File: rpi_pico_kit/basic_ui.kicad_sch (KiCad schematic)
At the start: 47 parts, among them Q3 BSS138, Q4 BSS138, Q5 BSS138, Q6 BSS138, SW2 RotaryEncoder_Switch, SW3 SW_Push_Dual, SW4 SW_Push_Dual, SW5 SW_Push_Dual, SW6 SW_Push_Dual, U5 74HC14

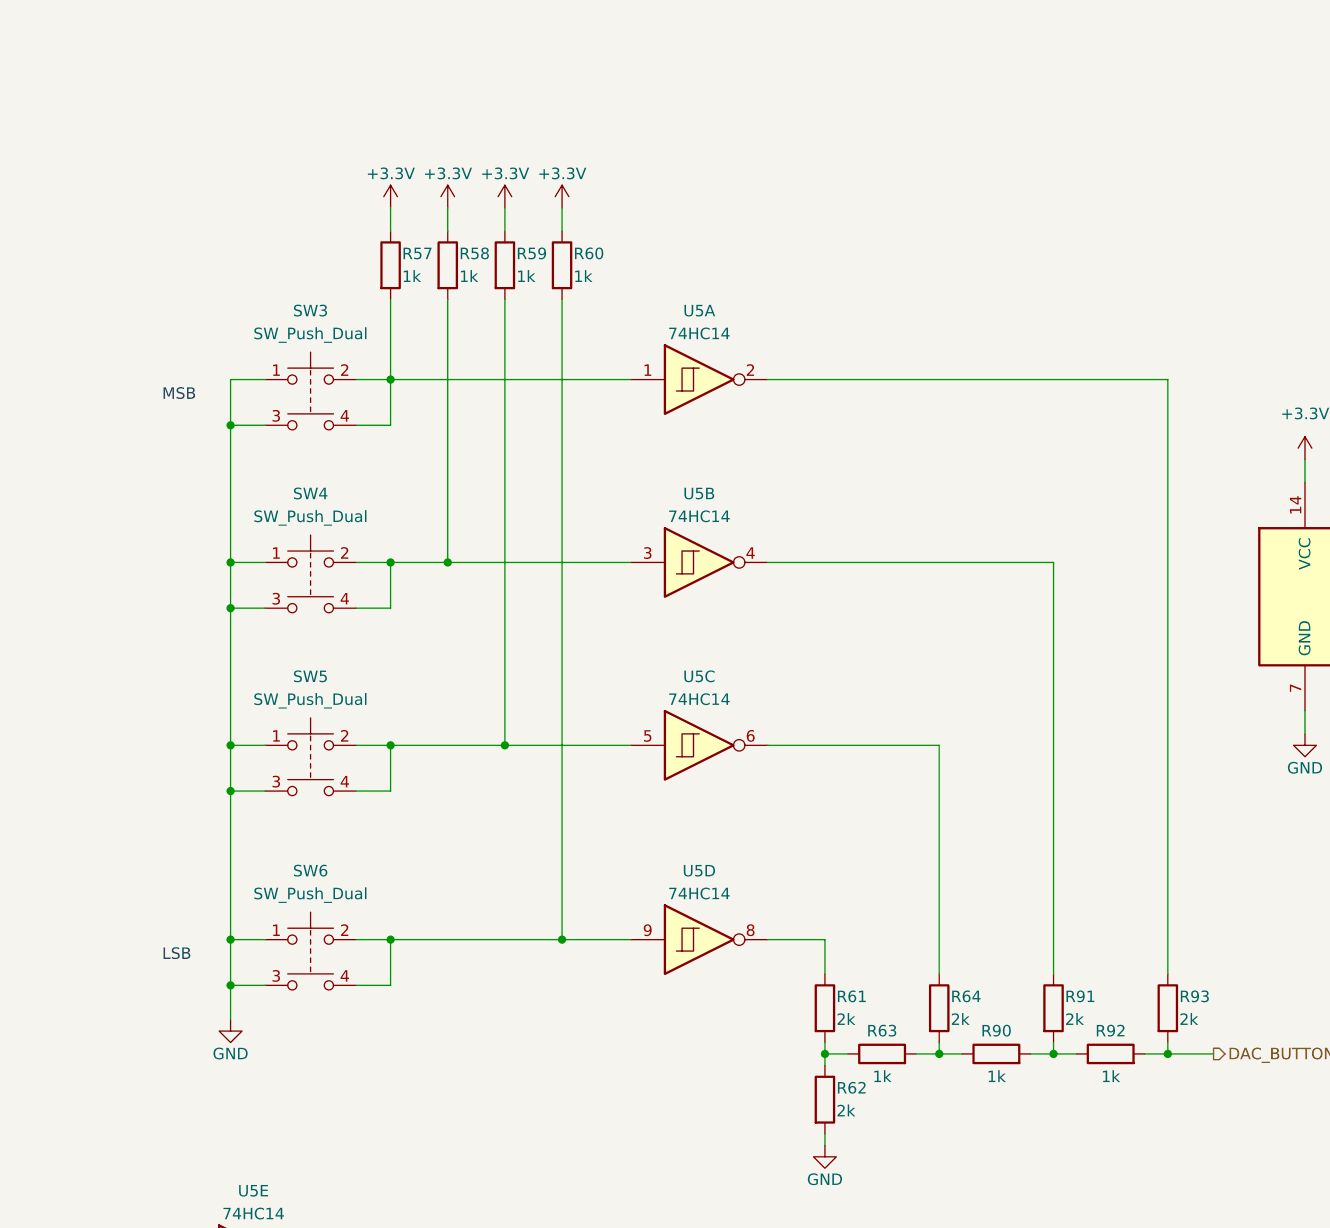
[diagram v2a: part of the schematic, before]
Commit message: replaced buttons in schematic
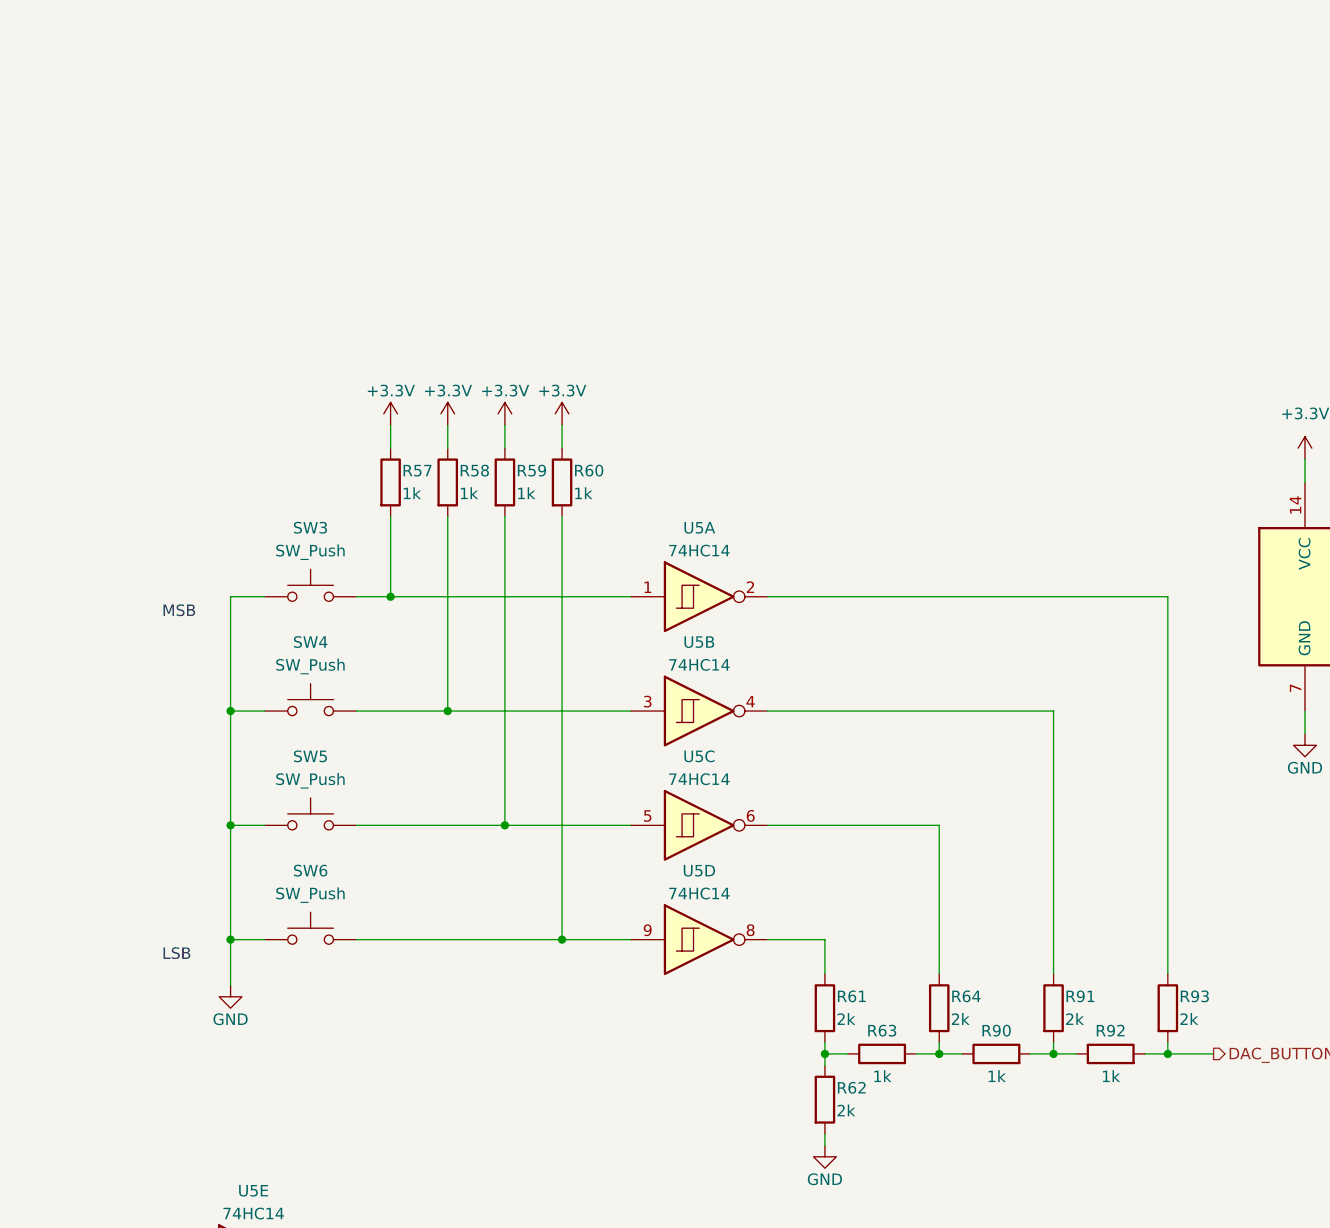
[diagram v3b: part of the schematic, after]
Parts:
- removed SW3, SW4, SW5, SW6: SW_Push_Dual, symbol Switch:SW_Push_Dual
- added SW3, SW4, SW5, SW6: SW_Push, Button_Switch_THT:SW_TH_Tactile_Omron_B3F-10xx, symbol Switch:SW_Push
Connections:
- net GND: now also SW3.1, SW4.1, SW5.1, SW6.1
- net at R60.2, U5.9: now also SW6.2
- net at R58.2, U5.3: now also SW4.2
- net at R57.2, U5.1: now also SW3.2
- net at R59.2, U5.5: now also SW5.2
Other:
- moved on the sheet: R57, R58, R59, R60, U5A, U5B, U5C

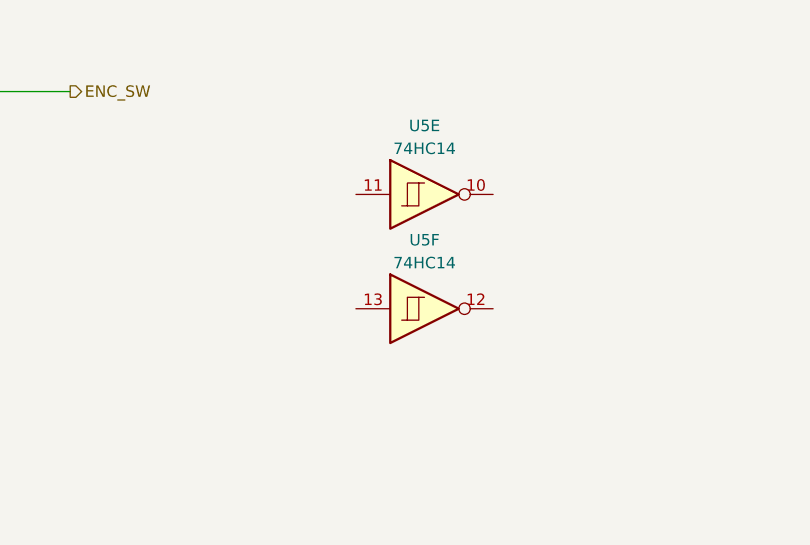
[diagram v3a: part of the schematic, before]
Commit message: connected unused logic gates to ground
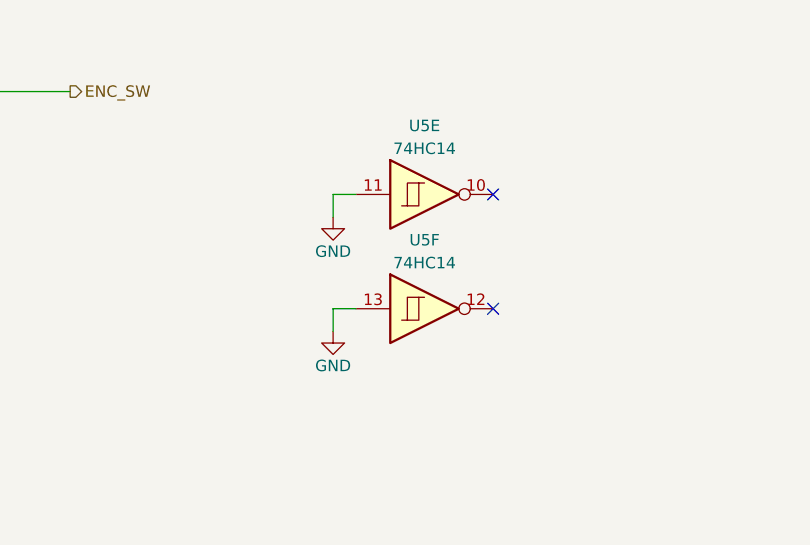
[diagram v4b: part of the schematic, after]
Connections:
- net GND: now also U5.11, U5.13
- no-connect marks 0 -> 2
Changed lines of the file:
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@@
   (junction (at 252.73 130.81) (diameter 0) (color 0 0 0 0)
   )
+  (no_connect (at 158.75 153.67))
+  (no_connect (at 158.75 166.37))
   (wire (pts (xy 102.87 30.48) (xy 102.87 33.02))
     (stroke (width 0) (type default))
@@
     (stroke (width 0) (type default))
   )
+  (wire (pts (xy 140.97 166.37) (xy 140.97 168.91))
+    (stroke (width 0) (type default))
+  )
   (wire (pts (xy 227.33 105.41) (xy 227.33 121.92))
     (stroke (width 0) (type default))
@@
     (stroke (width 0) (type default))
   )
+  (wire (pts (xy 143.51 166.37) (xy 140.97 166.37))
+    (stroke (width 0) (type default))
+  )
   (wire (pts (xy 102.87 60.96) (xy 102.87 53.34))
     (stroke (width 0) (type default))
@@
     (stroke (width 0) (type default))
   )
+  (wire (pts (xy 143.51 153.67) (xy 140.97 153.67))
+    (stroke (width 0) (type default))
+  )
   (wire (pts (xy 48.26 147.32) (xy 59.69 147.32))
     (stroke (width 0) (type default))
@@
   )
   (wire (pts (xy 50.8 20.32) (xy 50.8 22.86))
+    (stroke (width 0) (type default))
+  )
+  (wire (pts (xy 140.97 153.67) (xy 140.97 156.21))
     (stroke (width 0) (type default))
   )
@@
     )
     (property "Datasheet" "" (id 3) (at 50.8 60.96 0)
+      (effects (font (size 1.27 1.27)) hide)
+    )
+    (pin "1")
+  )
+  (symbol (lib_id "power:GND") (at 140.97 168.91 0) (unit 1)
+    (in_bom yes) (on_board yes)
+    (property "Reference" "#PWR0149" (id 0) (at 140.97 175.26 0)
+      (effects (font (size 1.27 1.27)) hide)
+    )
+    (property "Value" "GND" (id 1) (at 140.97 172.72 0)
+      (effects (font (size 1.27 1.27)))
+    )
+    (property "Footprint" "" (id 2) (at 140.97 168.91 0)
+      (effects (font (size 1.27 1.27)) hide)
+    )
+    (property "Datasheet" "" (id 3) (at 140.97 168.91 0)
       (effects (font (size 1.27 1.27)) hide)
     )
@@
       (effects (font (size 1.27 1.27)) hide)
     )
+    (pin "1")
+  )
+  (symbol (lib_id "power:GND") (at 140.97 156.21 0) (unit 1)
+    (in_bom yes) (on_board yes)
+    (property "Reference" "#PWR0148" (id 0) (at 140.97 162.56 0)
+      (effects (font (size 1.27 1.27)) hide)
+    )
+    (property "Value" "GND" (id 1) (at 140.97 160.02 0)
+      (effects (font (size 1.27 1.27)))
+    )
+    (property "Footprint" "" (id 2) (at 140.97 156.21 0)
+      (effects (font (size 1.27 1.27)) hide)
+    )
+    (property "Datasheet" "" (id 3) (at 140.97 156.21 0)
+      (effects (font (size 1.27 1.27)) hide)
+    )

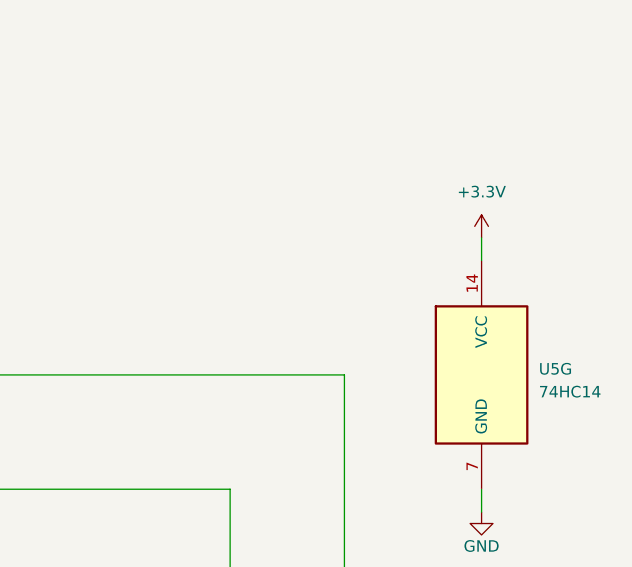
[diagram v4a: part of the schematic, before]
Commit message: added bypass capacitor to schmitt inverter
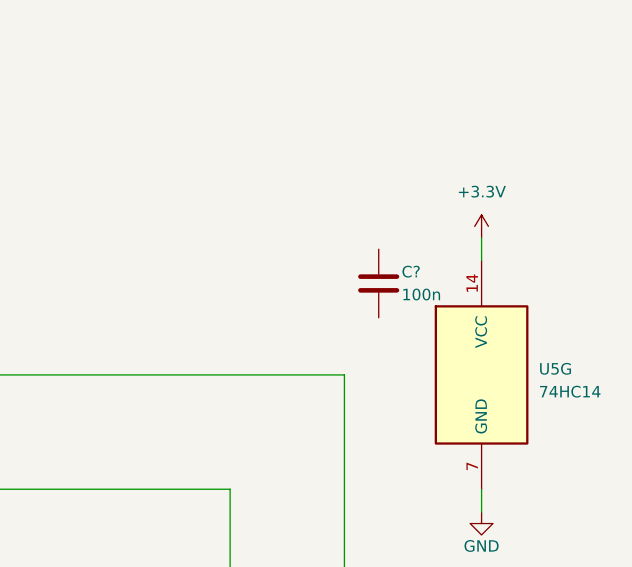
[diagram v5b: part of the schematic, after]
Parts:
- added C?: 100n, Capacitor_SMD:C_0805_2012Metric_Pad1.18x1.45mm_HandSolder, symbol Device:C
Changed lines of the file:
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@@
+    (pin "2")
+  )
+  (symbol (lib_id "Device:C") (at 256.54 69.85 180) (unit 1)
+    (in_bom yes) (on_board yes)
+    (property "Reference" "C?" (id 0) (at 259.08 68.58 0)
+      (effects (font (size 1.27 1.27)) (justify right))
+    )
+    (property "Value" "100n" (id 1) (at 259.08 71.12 0)
+      (effects (font (size 1.27 1.27)) (justify right))
+    )
+    (property "Footprint" "Capacitor_SMD:C_0805_2012Metric_Pad1.18x1.45mm_HandSolder" (id 2) (at 255.5748 66.04 0)
+      (effects (font (size 1.27 1.27)) hide)
+    )
+    (property "Datasheet" "~" (id 3) (at 256.54 69.85 0)
+      (effects (font (size 1.27 1.27)) hide)
+    )
+    (pin "1")
     (pin "2")
   )

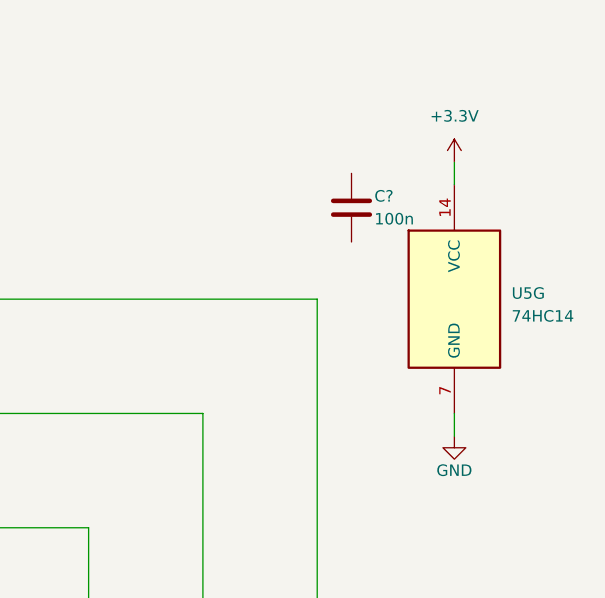
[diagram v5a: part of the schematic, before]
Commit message: changed schematic for uart leds
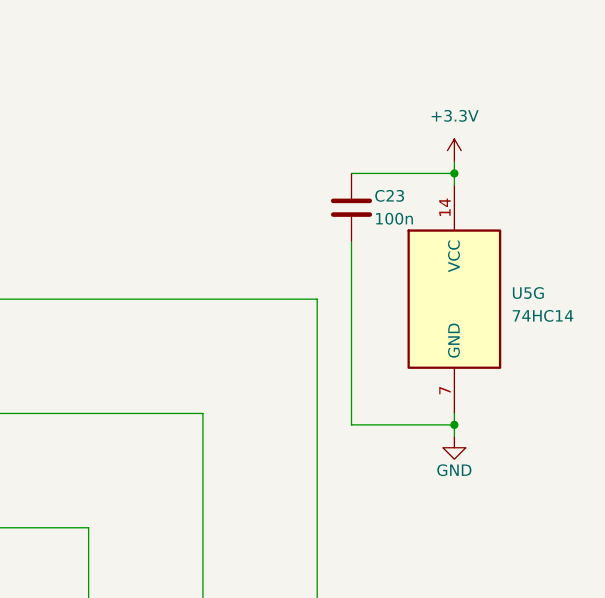
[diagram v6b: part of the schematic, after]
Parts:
- gave numbers to parts that had none: 1
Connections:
- net +3V3: now also C23.2
- net GND: now also C23.1
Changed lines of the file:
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@@
   (junction (at 179.07 105.41) (diameter 0) (color 0 0 0 0)
+  )
+  (junction (at 267.97 66.04) (diameter 0) (color 0 0 0 0)
+  )
+  (junction (at 267.97 93.98) (diameter 0) (color 0 0 0 0)
   )
   (junction (at 92.71 101.6) (diameter 0) (color 0 0 0 0)
@@
     (stroke (width 0) (type default))
   )
-  (wire (pts (xy 267.97 64.77) (xy 267.97 67.31))
+  (wire (pts (xy 267.97 64.77) (xy 267.97 66.04))
+    (stroke (width 0) (type default))
+  )
+  (wire (pts (xy 267.97 66.04) (xy 267.97 67.31))
     (stroke (width 0) (type default))
   )
@@
     (stroke (width 0) (type default))
   )
+  (wire (pts (xy 256.54 66.04) (xy 267.97 66.04))
+    (stroke (width 0) (type default))
+  )
   (wire (pts (xy 91.44 127) (xy 91.44 129.54))
     (stroke (width 0) (type default))
@@
     (stroke (width 0) (type default))
   )
+  (wire (pts (xy 256.54 93.98) (xy 267.97 93.98))
+    (stroke (width 0) (type default))
+  )
   (wire (pts (xy 92.71 48.26) (xy 92.71 50.8))
     (stroke (width 0) (type default))
@@
     (stroke (width 0) (type default))
   )
+  (wire (pts (xy 256.54 73.66) (xy 256.54 93.98))
+    (stroke (width 0) (type default))
+  )
   (wire (pts (xy 58.42 181.61) (xy 58.42 185.42))
     (stroke (width 0) (type default))
@@
     (stroke (width 0) (type default))
   )
-  (wire (pts (xy 267.97 95.25) (xy 267.97 92.71))
+  (wire (pts (xy 267.97 95.25) (xy 267.97 93.98))
     (stroke (width 0) (type default))
   )
@@
   )
   (wire (pts (xy 52.07 127) (xy 52.07 129.54))
+    (stroke (width 0) (type default))
+  )
+  (wire (pts (xy 267.97 93.98) (xy 267.97 92.71))
     (stroke (width 0) (type default))
   )
@@
   (symbol (lib_id "Device:C") (at 256.54 69.85 180) (unit 1)
     (in_bom yes) (on_board yes)
-    (property "Reference" "C?" (id 0) (at 259.08 68.58 0)
+    (property "Reference" "C23" (id 0) (at 259.08 68.58 0)
       (effects (font (size 1.27 1.27)) (justify right))
     )
